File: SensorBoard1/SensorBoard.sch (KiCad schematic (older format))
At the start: 20 parts

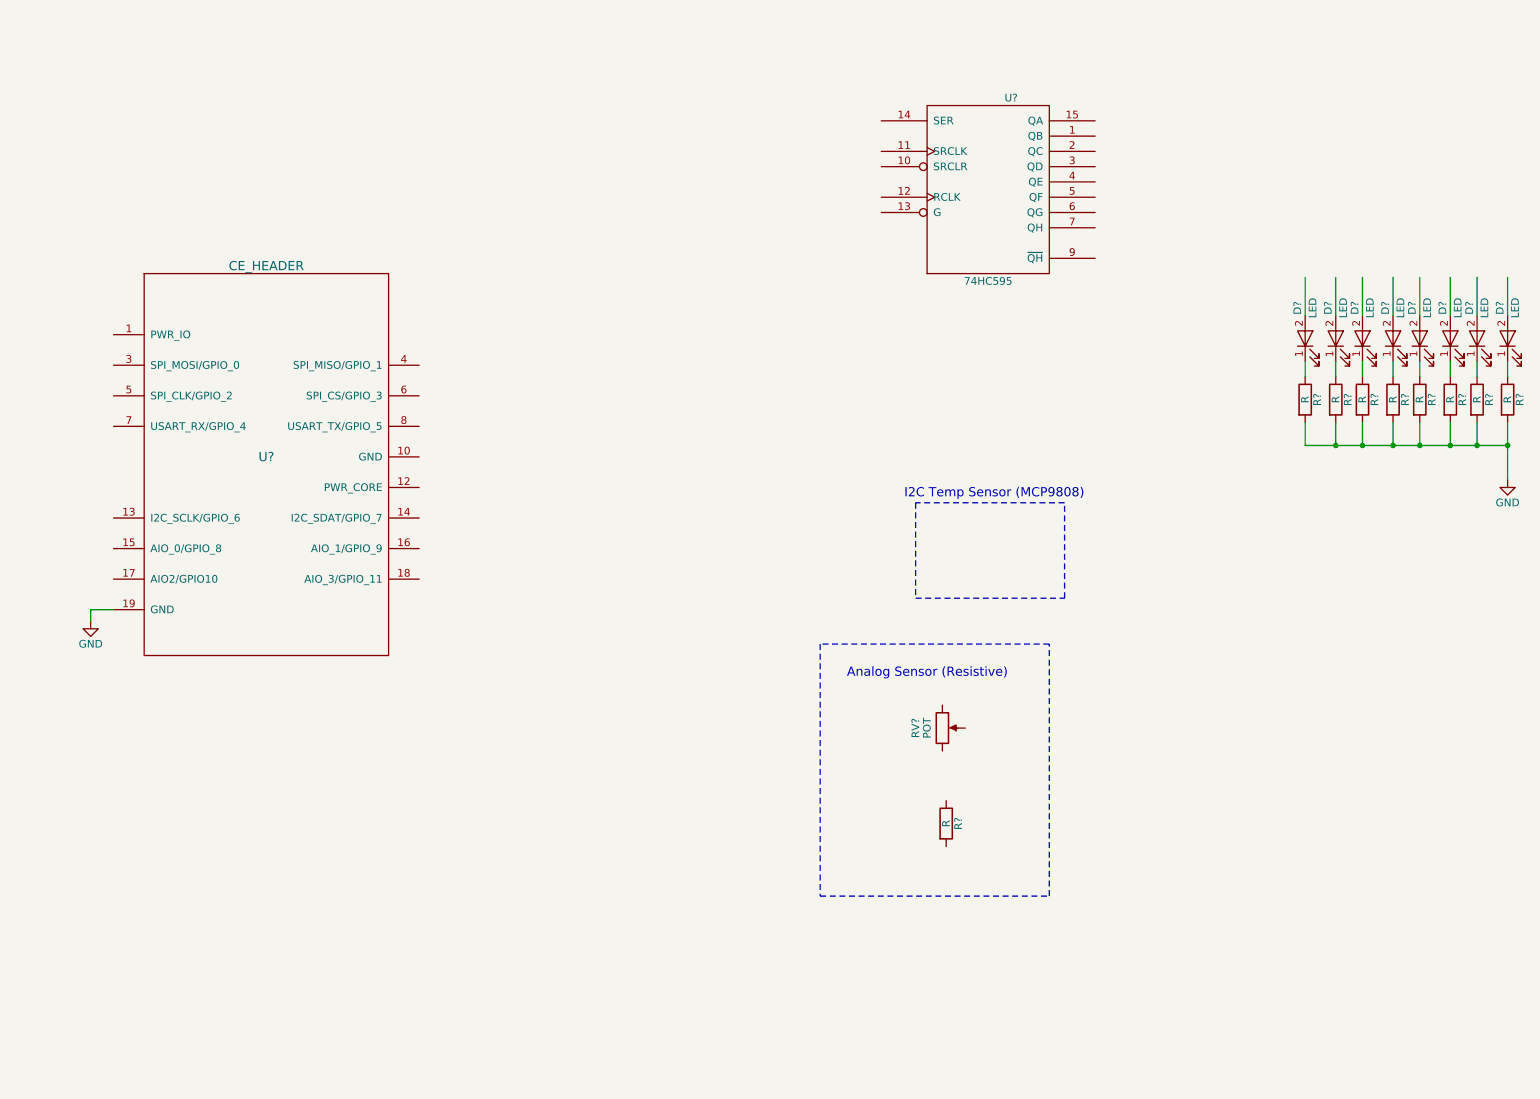
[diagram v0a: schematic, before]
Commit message: Created symbol for DS7505 temp sensor
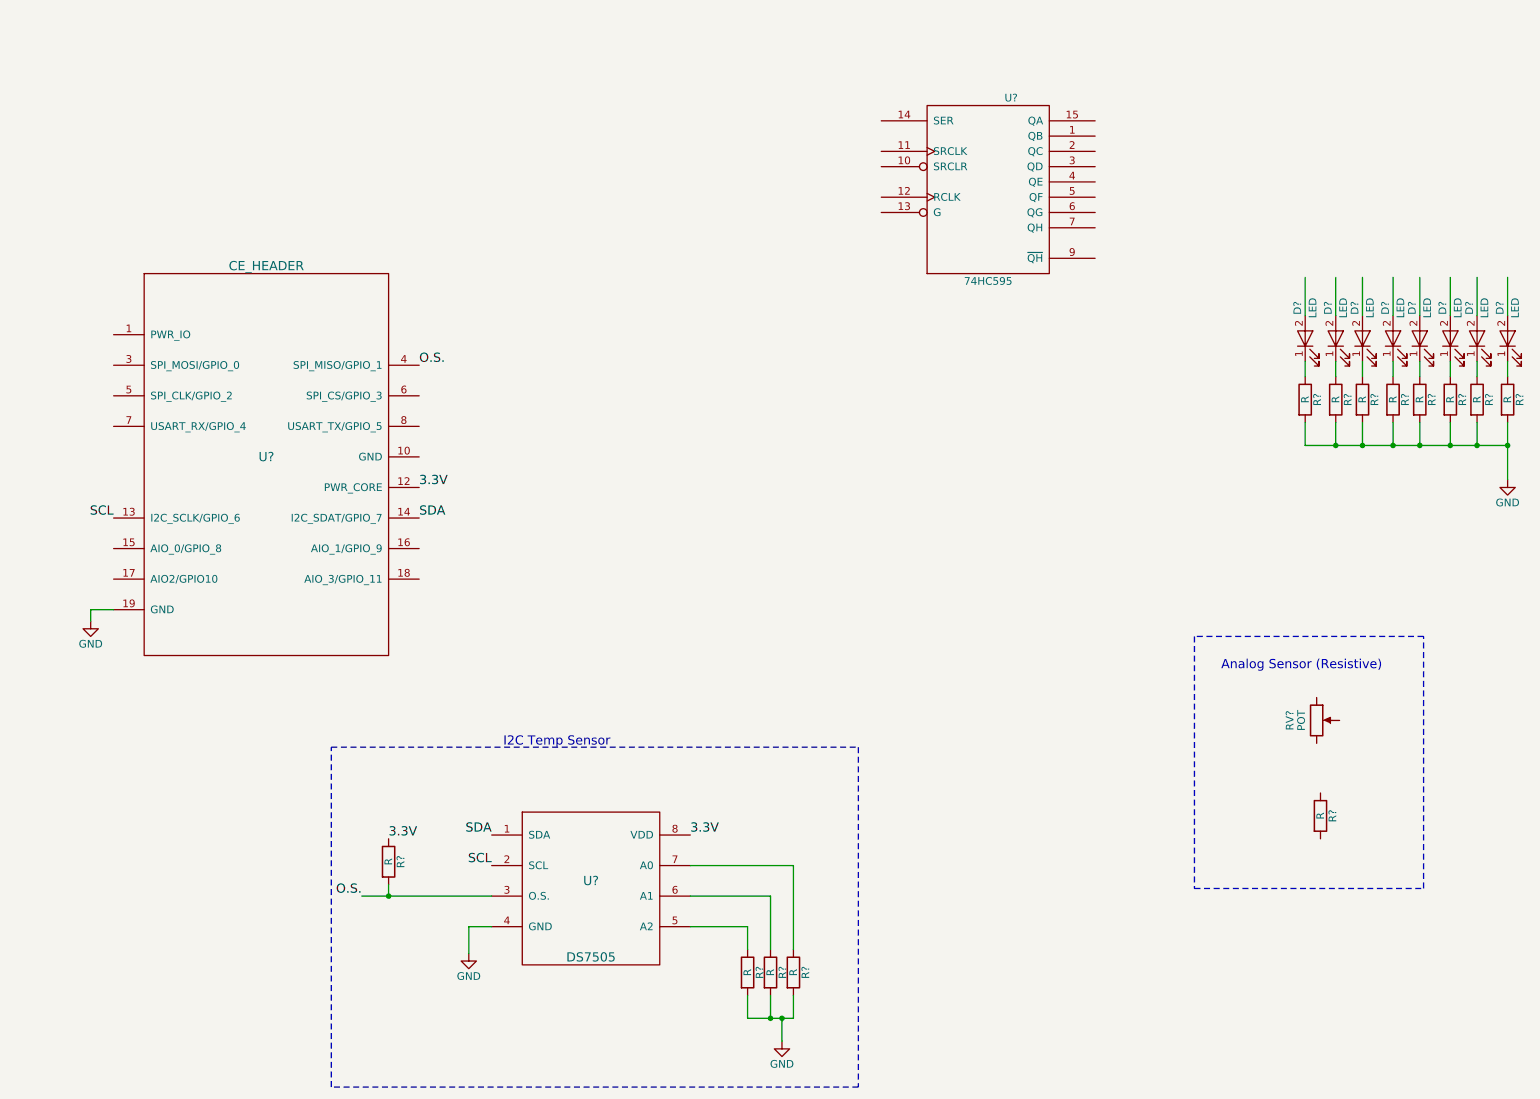
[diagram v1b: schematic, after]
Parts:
- added R? (x4): R, symbol R
- added U?: DS7505, symbol DS7505
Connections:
- net labels added: 3.3V, O.S., SCL, SDA
- wire segments 27 -> 42
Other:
- note added: "I2C Temp Sensor\n"
- note removed: "I2C Temp Sensor (MCP9808)"
- moved on the sheet: R?, RV?
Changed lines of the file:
@@
 LIBS:valves
 LIBS:ce_header
+LIBS:SensorBoard
+LIBS:SensorBoard-cache
 EELAYER 25 0
 EELAYER END
@@
 	9575 2825 9575 2925
 Wire Wire Line
-	10700 3225 10700 3375
+	10700 3375 10700 3225
 Wire Wire Line
 	9575 3375 10900 3375
@@
 L R R?
 U 1 1 58AE4015
-P 7225 5850
-F 0 "R?" V 7305 5850 50  0000 C CNN
-F 1 "R" V 7225 5850 50  0000 C CNN
-F 2 "" V 7155 5850 50  0000 C CNN
-F 3 "" H 7225 5850 50  0000 C CNN
-	1    7225 5850
+P 9675 5800
+F 0 "R?" V 9755 5800 50  0000 C CNN
+F 1 "R" V 9675 5800 50  0000 C CNN
+F 2 "" V 9605 5800 50  0000 C CNN
+F 3 "" H 9675 5800 50  0000 C CNN
+	1    9675 5800
 	1    0    0    -1
 $EndComp
@@
 L POT RV?
 U 1 1 58AE409A
-P 7200 5225
-F 0 "RV?" V 7025 5225 50  0000 C CNN
-F 1 "POT" V 7100 5225 50  0000 C CNN
-F 2 "" H 7200 5225 50  0000 C CNN
-F 3 "" H 7200 5225 50  0000 C CNN
-	1    7200 5225
-	1    0    0    -1
-$EndComp
-Wire Notes Line
-	6400 4675 6400 6325
-Wire Notes Line
-	6400 6325 7900 6325
-Wire Notes Line
-	7900 6325 7900 4675
-Wire Notes Line
-	7900 4675 6400 4675
-Text Notes 6575 4900 0    60   ~ 0
+P 9650 5175
+F 0 "RV?" V 9475 5175 50  0000 C CNN
+F 1 "POT" V 9550 5175 50  0000 C CNN
+F 2 "" H 9650 5175 50  0000 C CNN
+F 3 "" H 9650 5175 50  0000 C CNN
+	1    9650 5175
+	1    0    0    -1
+$EndComp
+Wire Notes Line
+	8850 4625 8850 6275
+Wire Notes Line
+	8850 6275 10350 6275
+Wire Notes Line
+	10350 6275 10350 4625
+Wire Notes Line
+	10350 4625 8850 4625
+Text Notes 9025 4850 0    60   ~ 0
 Analog Sensor (Resistive)
-Wire Notes Line
-	7025 3750 7025 4375
-Wire Notes Line
-	7025 4375 8000 4375
-Wire Notes Line
-	8000 4375 8000 3750
-Wire Notes Line
-	8000 3750 7025 3750
-Text Notes 6950 3725 0    60   ~ 0
-I2C Temp Sensor (MCP9808)
+Text Notes 4325 5350 0    60   ~ 0
+I2C Temp Sensor\n
 $Comp
 L GND #PWR?
@@
 Wire Wire Line
 	1625 4450 1775 4450
+$Comp
+L DS7505 U?
+U 1 1 58AF5CB3
+P 4900 6225
+F 0 "U?" H 4900 6225 60  0000 C CNN
+F 1 "DS7505" H 4900 5725 60  0000 C CNN
+F 2 "" H 4950 6225 60  0001 C CNN
+F 3 "" H 4950 6225 60  0001 C CNN
+	1    4900 6225
+	1    0    0    -1
+$EndComp
+Text Label 4250 5925 2    60   ~ 0
+SDA
+Text Label 4250 6125 2    60   ~ 0
+SCL
+$Comp
+L R R?
+U 1 1 58AF6DB0
+P 6225 6825
+F 0 "R?" V 6305 6825 50  0000 C CNN
+F 1 "R" V 6225 6825 50  0000 C CNN
+F 2 "" V 6155 6825 50  0000 C CNN
+F 3 "" H 6225 6825 50  0000 C CNN
+	1    6225 6825
+	1    0    0    -1
+$EndComp
+$Comp
+L R R?
+U 1 1 58AF70A8
+P 6075 6825
+F 0 "R?" V 6155 6825 50  0000 C CNN
+F 1 "R" V 6075 6825 50  0000 C CNN
+F 2 "" V 6005 6825 50  0000 C CNN
+F 3 "" H 6075 6825 50  0000 C CNN
+	1    6075 6825
+	1    0    0    -1
+$EndComp
+$Comp
+L R R?
+U 1 1 58AF710B
+P 5925 6825
+F 0 "R?" V 6005 6825 50  0000 C CNN
+F 1 "R" V 5925 6825 50  0000 C CNN
+F 2 "" V 5855 6825 50  0000 C CNN
+F 3 "" H 5925 6825 50  0000 C CNN
+	1    5925 6825
+	1    0    0    -1
+$EndComp
+Wire Wire Line
+	5925 6675 5925 6525
+Wire Wire Line
+	5925 6525 5550 6525
+Wire Wire Line
+	5550 6325 6075 6325
+Wire Wire Line
+	6075 6325 6075 6675
+Wire Wire Line
+	6225 6675 6225 6125
+Wire Wire Line
+	6225 6125 5550 6125
+Wire Wire Line
+	5925 6975 5925 7125
+Wire Wire Line
+	5925 7125 6225 7125
+Wire Wire Line
+	6225 7125 6225 6975
+Wire Wire Line
+	6075 6975 6075 7125
+Connection ~ 6075 7125
+Wire Wire Line
+	6150 7125 6150 7275
+Connection ~ 6150 7125
+$Comp
+L GND #PWR?
+U 1 1 58AF7AD0
+P 6150 7275
+F 0 "#PWR?" H 6150 7025 50  0001 C CNN
+F 1 "GND" H 6150 7125 50  0000 C CNN
+F 2 "" H 6150 7275 50  0000 C CNN
+F 3 "" H 6150 7275 50  0000 C CNN
+	1    6150 7275
+	1    0    0    -1
+$EndComp
+Text Label 3775 3650 0    60   ~ 0
+3.3V
+Text Label 5550 5925 0    60   ~ 0
+3.3V
+$Comp
+L GND #PWR?
+U 1 1 58AF88AD
+P 4100 6700
+F 0 "#PWR?" H 4100 6450 50  0001 C CNN
+F 1 "GND" H 4100 6550 50  0000 C CNN
+F 2 "" H 4100 6700 50  0000 C CNN
+F 3 "" H 4100 6700 50  0000 C CNN
+	1    4100 6700
+	1    0    0    -1
+$EndComp
+Wire Wire Line
+	4100 6700 4100 6525
+Wire Wire Line
+	4100 6525 4250 6525
+Text Label 3775 2850 0    60   ~ 0
+O.S.
+Text Label 3400 6325 2    60   ~ 0
+O.S.
+Wire Wire Line
+	4250 6325 3400 6325
+$Comp
+L R R?
+U 1 1 58AFA0D7
+P 3575 6100
+F 0 "R?" V 3655 6100 50  0000 C CNN
+F 1 "R" V 3575 6100 50  0000 C CNN
+F 2 "" V 3505 6100 50  0000 C CNN
+F 3 "" H 3575 6100 50  0000 C CNN
+	1    3575 6100
+	1    0    0    -1
+$EndComp
+Wire Wire Line
+	3575 6250 3575 6325
+Connection ~ 3575 6325
+Text Label 3575 5950 0    60   ~ 0
+3.3V
+Wire Notes Line
+	6650 5350 6650 7575
+Wire Notes Line
+	6650 7575 3200 7575
+Wire Notes Line
+	3200 7575 3200 5350
+Wire Notes Line
+	3200 5350 6650 5350
+Text Label 3775 3850 0    60   ~ 0
+SDA
+Text Label 1775 3850 2    60   ~ 0
+SCL
 $EndSCHEMATC

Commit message: Finished schematic for small sensor board
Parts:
- removed RV?: POT, symbol POT
- removed U?: 74HC595, symbol 74HC595
- added C? (x3): C, symbol C
- added R?: Photo Resistor, symbol R_PHOTO
- added R?: R, symbol R
- added U?: 74HC595-PWR, symbol 74HC595-PWR
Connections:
- net labels added: 5V, PR_BOT, PR_TOP, clockPin, dataPin, latchPin
- wire segments 42 -> 75
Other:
- moved on the sheet: R?

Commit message: Associated footprints
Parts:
- C1, C2, C3: renamed from C?; footprint (none) -> Capacitors_SMD:C_0805
- D1, D2, D3, D4, D5, D6, D7, D8: renamed from D?; footprint (none) -> LEDs:LED_0805
- R1, R10, R11, R12, R13, R14, R15, R2, R3, R4, R5, R7, R8, R9: renamed from R?; footprint (none) -> Resistors_SMD:R_0805
- R6: renamed from R?; footprint (none) -> Capacitors_ThroughHole:CP_Radial_Tantal_D5.5mm_P5.00mm
- U1: renamed from U?; footprint (none) -> SensorBoard:CE_Header
- U2: renamed from U?; footprint (none) -> Housings_SOIC:SOIC-8-1EP_3.9x4.9mm_Pitch1.27mm
- U3: renamed from U?; footprint (none) -> Housings_SOIC:SOIC-16_3.9x9.9mm_Pitch1.27mm
